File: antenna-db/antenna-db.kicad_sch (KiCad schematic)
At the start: 5 parts, among them J1 PC104_Connector

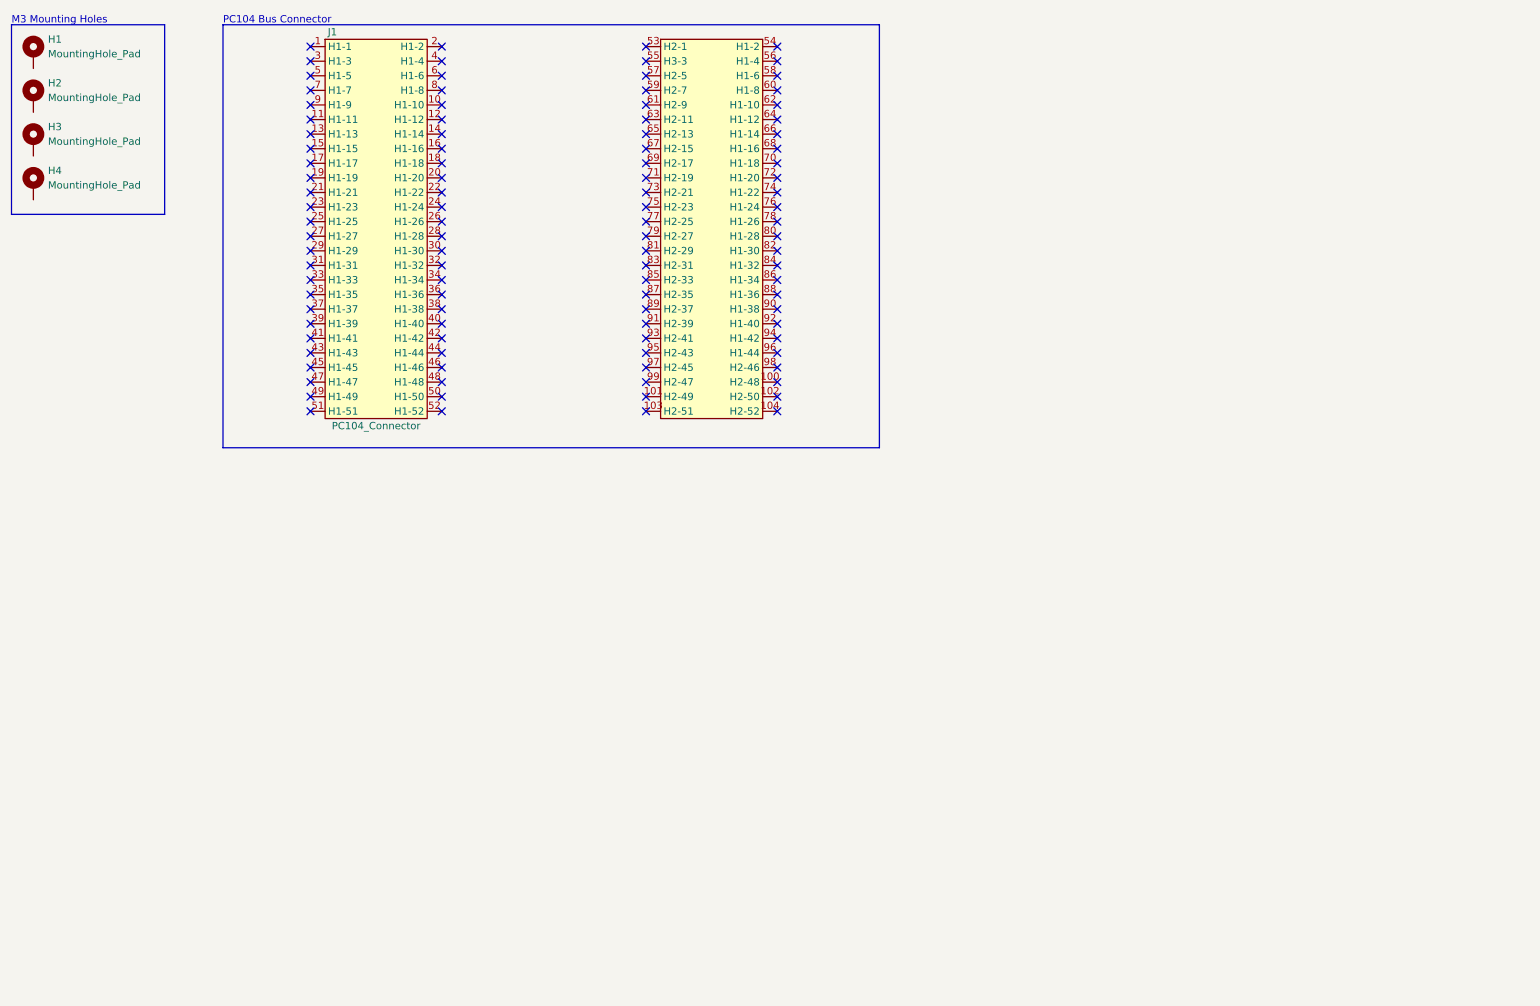
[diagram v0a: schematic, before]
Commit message: added temp sensor & porgamming/test connections
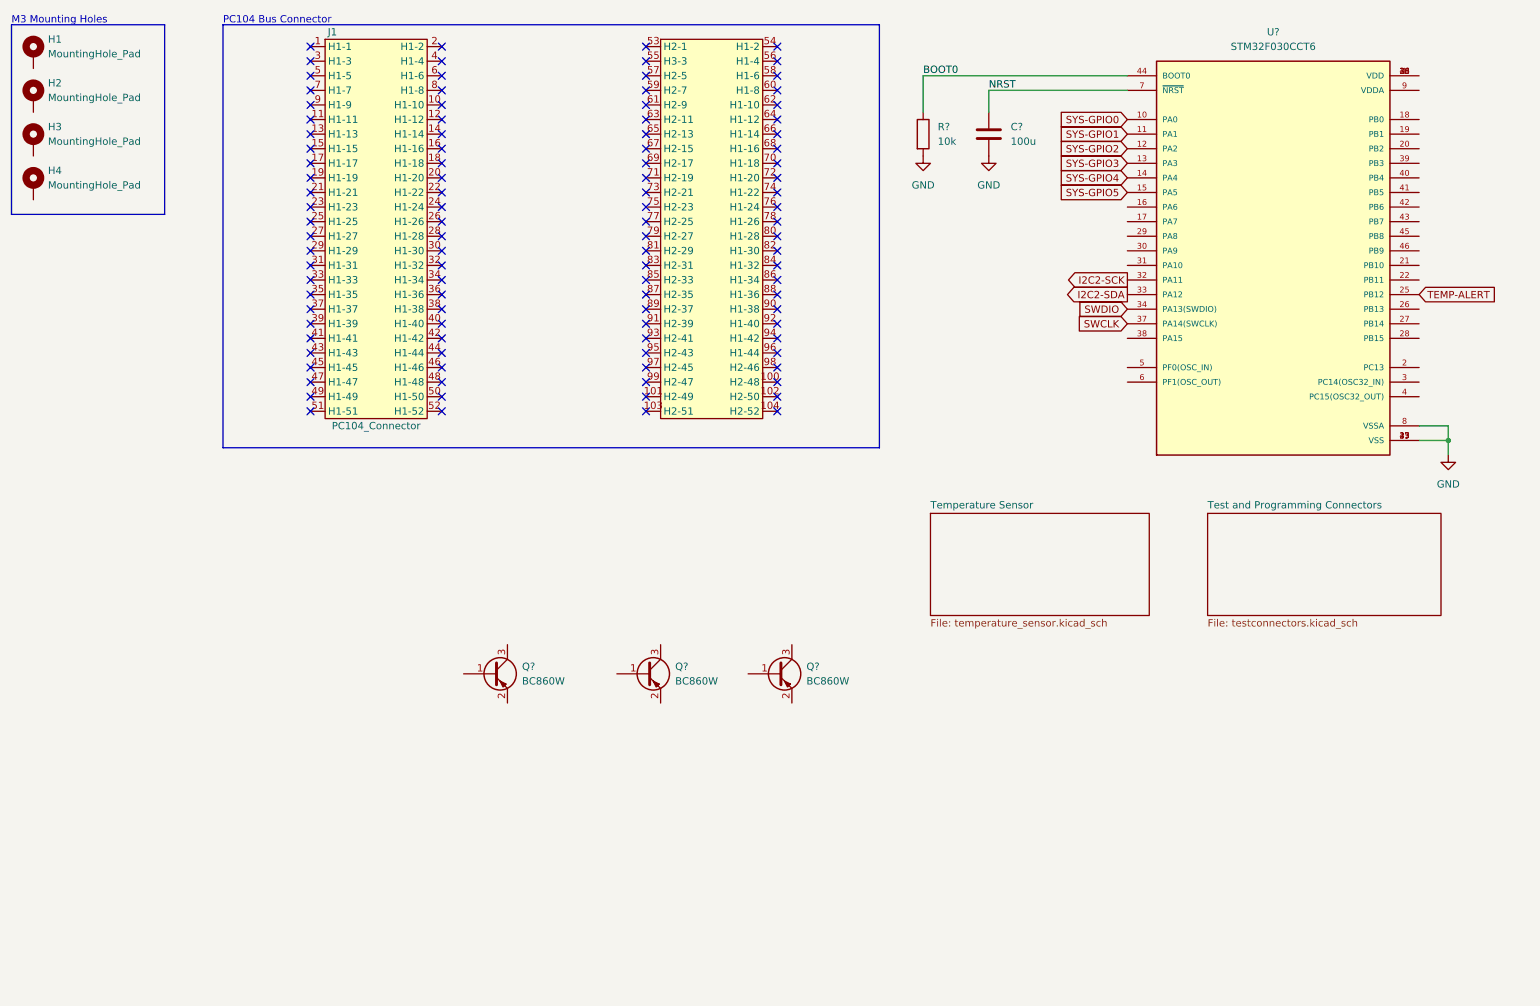
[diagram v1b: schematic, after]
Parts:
- added C?: 100u, symbol Device:C
- added Q? (x3): BC860W, Package_TO_SOT_SMD:SOT-323_SC-70, symbol Transistor_BJT:BC860W
- added R?: 10k, symbol Device:R
- added U?: STM32F030CCT6, QFP50P900X900X160-48N, symbol STM32F030CCT6:STM32F030CCT6
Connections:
- new net: U?.1 (VDD), U?.24 (VDD), U?.36 (VDD), U?.48 (VDD)
- new net BOOT0: R?.1, U?.44 (BOOT0)
- new net GND: C?.2, R?.2, U?.23 (VSS), U?.35 (VSS), U?.47 (VSS), U?.8 (VSSA)
- new net I2C2-SCK: U?.32 (PA11)
- new net I2C2-SDA: U?.33 (PA12)
- new net NRST: C?.1, U?.7 (~{NRST})
- new net SWCLK: U?.37 (PA14(SWCLK))
- new net SWDIO: U?.34 (PA13(SWDIO))
- new net SYS-GPIO0: U?.10 (PA0)
- new net SYS-GPIO1: U?.11 (PA1)
- new net SYS-GPIO2: U?.12 (PA2)
- new net SYS-GPIO3: U?.13 (PA3)
- new net SYS-GPIO4: U?.14 (PA4)
- new net SYS-GPIO5: U?.15 (PA5)
- new net TEMP-ALERT: U?.25 (PB12)
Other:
- added sheet Temperature Sensor (temperature_sensor.kicad_sch)
- added sheet Test and Programming Connectors (testconnectors.kicad_sch)

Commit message: added bjts, pads
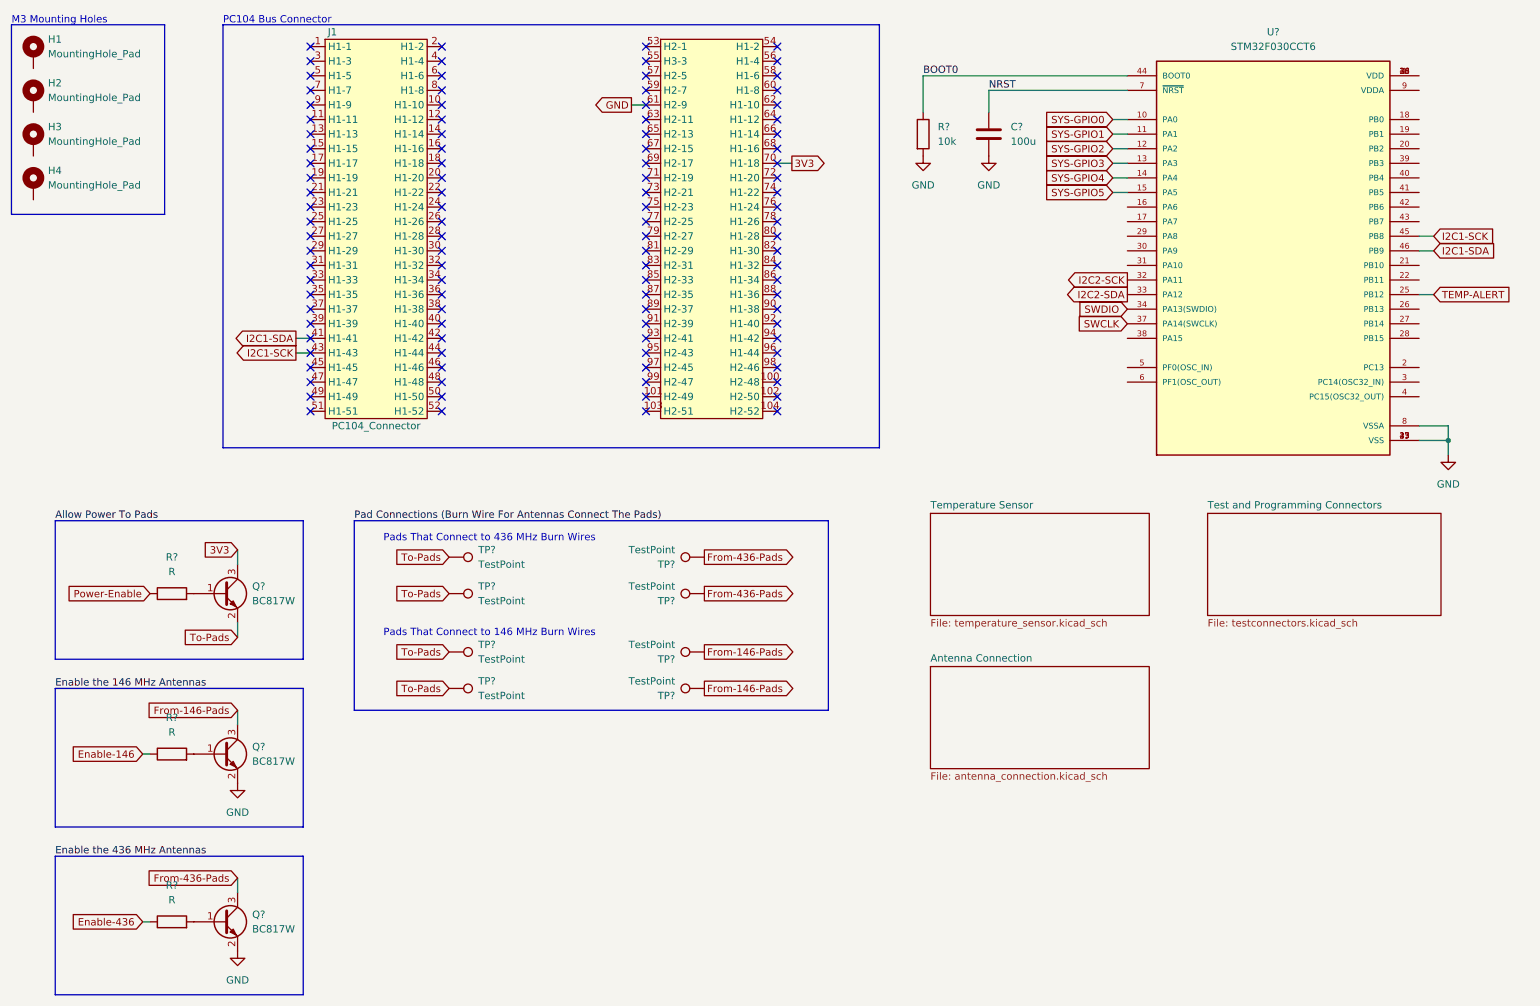
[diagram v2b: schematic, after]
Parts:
- removed Q? (x3): BC860W, Package_TO_SOT_SMD:SOT-323_SC-70, symbol Transistor_BJT:BC860W
- added Q? (x3): BC817W, Package_TO_SOT_SMD:SOT-323_SC-70, symbol Transistor_BJT:BC817W
- added R? (x3): R, symbol Device:R
- added TP? (x8): TestPoint, symbol Connector:TestPoint
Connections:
- net GND: now also J1.61 (H2-9), Q?.2 (E), Q?.2 (E)
- net I2C1-SCK: now reaches U?.45 (PB8)
- net I2C1-SCK: now also J1.43 (H1-43)
- net I2C1-SDA: now reaches U?.46 (PB9)
- net I2C1-SDA: now also J1.41 (H1-41)
- net 3V3: now reaches J1.70 (H1-18)
- net 3V3: now also Q?.3 (C)
- new net: Q?.1 (B), R?.2 (x3)
- new net Enable-146: R?.1
- new net Enable-436: R?.1
- new net From-146-Pads: Q?.3 (C), TP?.1, TP?.1
- new net From-436-Pads: Q?.3 (C), TP?.1, TP?.1
- new net Power-Enable: R?.1
- new net To-Pads: Q?.2 (E), TP?.1, TP?.1, TP?.1, TP?.1
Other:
- added sheet Antenna Connection (antenna_connection.kicad_sch)
- note added: "Pads That Connect to 146 MHz Burn Wires"
- note added: "Pads That Connect to 436 MHz Burn Wires"

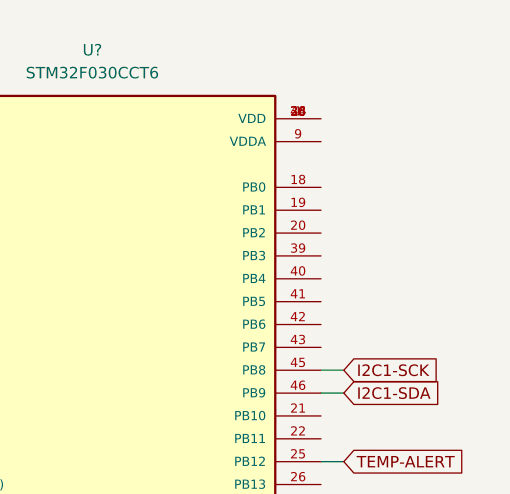
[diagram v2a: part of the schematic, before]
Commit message: added mcu connections
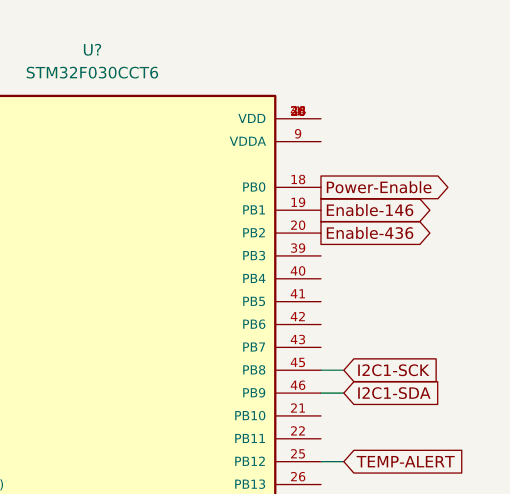
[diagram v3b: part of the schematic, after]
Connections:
- net Enable-146: now also U?.19 (PB1)
- net Enable-436: now also U?.20 (PB2)
- net Power-Enable: now also U?.18 (PB0)
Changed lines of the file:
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@@
+    )
+  )
+  (global_label "Power-Enable" (shape output) (at 259.08 31.75 0) (fields_autoplaced)
+    (effects (font (size 1.27 1.27)) (justify left))
+    (property "Intersheet References" "${INTERSHEET_REFS}" (id 0) (at 275.0398 31.6706 0)
+      (effects (font (size 1.27 1.27)) (justify left) hide)
     )
   )
@@
     )
   )
+  (global_label "Enable-146" (shape output) (at 259.08 34.29 0) (fields_autoplaced)
+    (effects (font (size 1.27 1.27)) (justify left))
+    (property "Intersheet References" "${INTERSHEET_REFS}" (id 0) (at 273.0441 34.2106 0)
+      (effects (font (size 1.27 1.27)) (justify left) hide)
+    )
+  )
   (global_label "3V3" (shape input) (at 53.34 106.68 180) (fields_autoplaced)
     (effects (font (size 1.27 1.27)) (justify right))
@@
       (effects (font (size 1.27 1.27)) (justify left) hide)
     )
+  )
+  (global_label "Enable-436" (shape output) (at 259.08 36.83 0) (fields_autoplaced)
+    (effects (font (size 1.27 1.27)) (justify left))
+    (property "Intersheet References" "${INTERSHEET_REFS}" (id 0) (at 273.0441 36.7506 0)
+      (effects (font (size 1.27 1.27)) (justify left) hide)
+    )

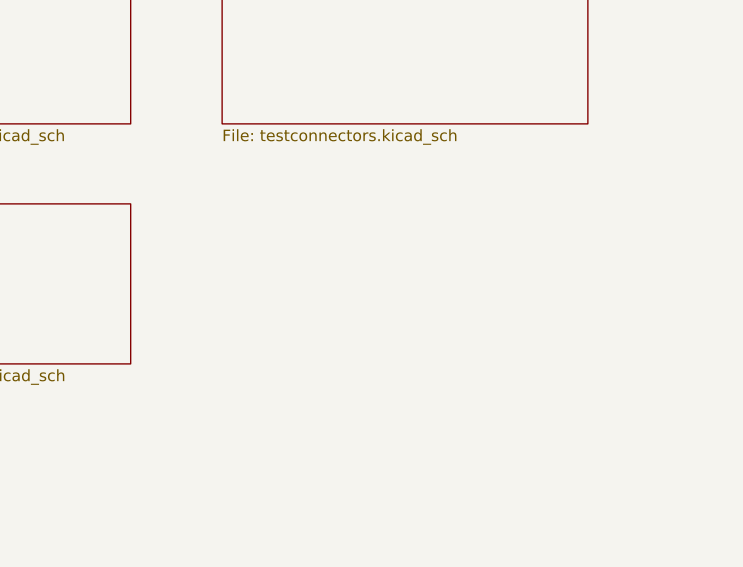
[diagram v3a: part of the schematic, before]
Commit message: added mounting holes
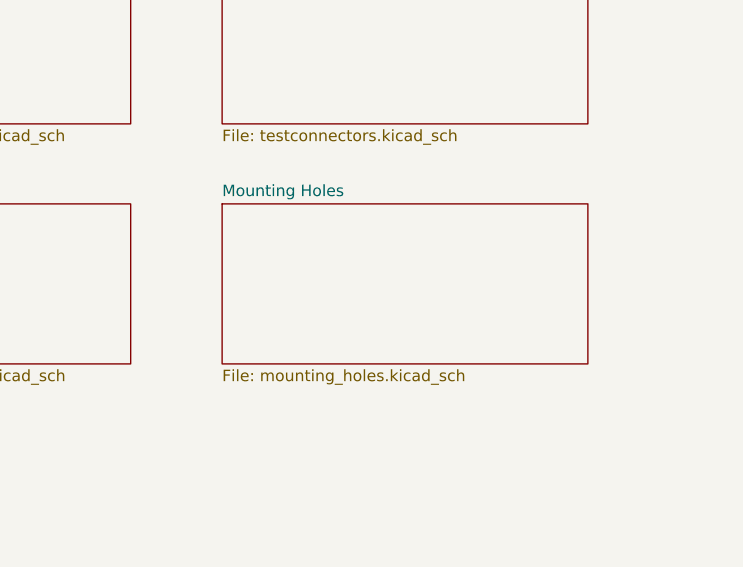
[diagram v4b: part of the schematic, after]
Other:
- added sheet Mounting Holes (mounting_holes.kicad_sch)
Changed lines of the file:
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@@
+    )
+  )
+  (sheet (at 222.25 127) (size 40.64 17.78) (fields_autoplaced)
+    (stroke (width 0.1524) (type solid) (color 0 0 0 0))
+    (fill (color 0 0 0 0.0000))
+    (property "Sheet name" "Mounting Holes" (id 0) (at 222.25 126.2884 0)
+      (effects (font (size 1.27 1.27)) (justify left bottom))
+    )
+    (property "Sheet file" "mounting_holes.kicad_sch" (id 1) (at 222.25 145.3646 0)
+      (effects (font (size 1.27 1.27)) (justify left top))
     )
   )
@@
     (path "/54ac4994-5c0a-4a36-bd0d-1a3e8e6525a3" (page "3"))
     (path "/22c3f5f3-512d-4f46-9e61-fd1ba62026f1" (page "4"))
+    (path "/fe959ac9-6dcb-4cd3-8c33-c42c0ff1718e" (page "5"))
   )
   (symbol_instances
@@
       (reference "H4") (unit 1) (value "MountingHole_Pad") (footprint "MountingHole:MountingHole_3.2mm_M3_Pad_TopBottom")
     )
+    (path "/fe959ac9-6dcb-4cd3-8c33-c42c0ff1718e/09a35508-1e1d-4152-b26d-be55aa6b6db3"
+      (reference "H?") (unit 1) (value "2.1mm") (footprint "")
+    )
+    (path "/fe959ac9-6dcb-4cd3-8c33-c42c0ff1718e/25a274b7-7989-4d0c-b91e-4969490caf32"
+      (reference "H?") (unit 1) (value "2.1mm") (footprint "")
+    )
+    (path "/fe959ac9-6dcb-4cd3-8c33-c42c0ff1718e/31412524-57ac-43e0-8c0a-6e35f0e397f4"
+      (reference "H?") (unit 1) (value "2.1mm") (footprint "")
+    )
+    (path "/fe959ac9-6dcb-4cd3-8c33-c42c0ff1718e/34a1dceb-785b-431c-a3b5-5c4cc2dc07e2"
+      (reference "H?") (unit 1) (value "2.1mm") (footprint "")
+    )
+    (path "/fe959ac9-6dcb-4cd3-8c33-c42c0ff1718e/35d6f3d0-c8c1-44fe-ad3f-4cf5a338b710"
+      (reference "H?") (unit 1) (value "2.1mm") (footprint "")
+    )
+    (path "/fe959ac9-6dcb-4cd3-8c33-c42c0ff1718e/3b6b224d-43c1-42c8-9f1a-45115e99adab"
+      (reference "H?") (unit 1) (value "2.1mm") (footprint "")
+    )
+    (path "/fe959ac9-6dcb-4cd3-8c33-c42c0ff1718e/4f2d515e-a7a2-44b8-a210-db688a47e996"
+      (reference "H?") (unit 1) (value "2.1mm") (footprint "")
+    )
+    (path "/fe959ac9-6dcb-4cd3-8c33-c42c0ff1718e/5927d759-5e6c-421b-a730-4349503e98c5"
+      (reference "H?") (unit 1) (value "2.1mm") (footprint "")
+    )
+    (path "/fe959ac9-6dcb-4cd3-8c33-c42c0ff1718e/5c650396-a68c-4db5-b24b-e1c29ebd7772"
+      (reference "H?") (unit 1) (value "2.1mm") (footprint "")
+    )
+    (path "/fe959ac9-6dcb-4cd3-8c33-c42c0ff1718e/601c86fa-f883-4953-8ab5-0f97df8588a3"
+      (reference "H?") (unit 1) (value "2.1mm") (footprint "")
+    )
+    (path "/fe959ac9-6dcb-4cd3-8c33-c42c0ff1718e/6a2347d5-3ff2-4d0e-803b-1128686a2e11"
+      (reference "H?") (unit 1) (value "2.1mm") (footprint "")
+    )
+    (path "/fe959ac9-6dcb-4cd3-8c33-c42c0ff1718e/7d1fabed-ffed-41d7-bbac-7eecfdbf19b1"
+      (reference "H?") (unit 1) (value "2.1mm") (footprint "")
+    )
+    (path "/fe959ac9-6dcb-4cd3-8c33-c42c0ff1718e/9055cf47-3f5e-47d1-a306-829e6afe1f28"
+      (reference "H?") (unit 1) (value "2.1mm") (footprint "")
+    )
+    (path "/fe959ac9-6dcb-4cd3-8c33-c42c0ff1718e/97f0a9dc-4ce6-4df9-9562-605a30b3750d"
+      (reference "H?") (unit 1) (value "2.1mm") (footprint "")
+    )
+    (path "/fe959ac9-6dcb-4cd3-8c33-c42c0ff1718e/9eac51c9-5d8c-4bd6-bc6c-f273d9c4bfa6"
+      (reference "H?") (unit 1) (value "2.1mm") (footprint "")
+    )
+    (path "/fe959ac9-6dcb-4cd3-8c33-c42c0ff1718e/ac347fcc-f0c8-49f0-b860-b46e0e785efd"
+      (reference "H?") (unit 1) (value "2.1mm") (footprint "")
+    )
+    (path "/fe959ac9-6dcb-4cd3-8c33-c42c0ff1718e/bbe1f1b4-8277-4fec-95cf-7bca8712c612"
+      (reference "H?") (unit 1) (value "2.1mm") (footprint "")
+    )
+    (path "/fe959ac9-6dcb-4cd3-8c33-c42c0ff1718e/c28a9993-5bd4-4efb-bb19-0c1d0b451da6"
+      (reference "H?") (unit 1) (value "2.1mm") (footprint "")
+    )
+    (path "/fe959ac9-6dcb-4cd3-8c33-c42c0ff1718e/cfae9fe8-f2ce-4bf5-924c-4e7f7c6a9de0"
+      (reference "H?") (unit 1) (value "2.1mm") (footprint "")
+    )
+    (path "/fe959ac9-6dcb-4cd3-8c33-c42c0ff1718e/eca82934-2ff4-42dd-96f1-1eca0afc421f"
+      (reference "H?") (unit 1) (value "2.1mm") (footprint "")
+    )
     (path "/e31ce43e-c5bc-45af-b896-73f32b15b5d8"
